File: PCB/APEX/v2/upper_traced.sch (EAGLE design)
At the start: 9 parts

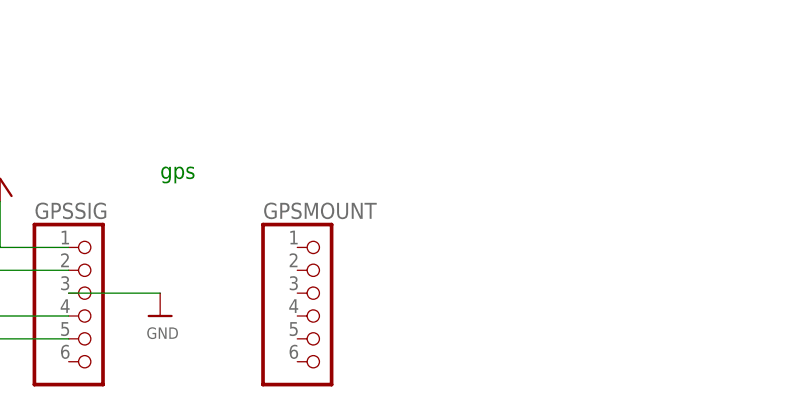
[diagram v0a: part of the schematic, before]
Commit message: realign sim
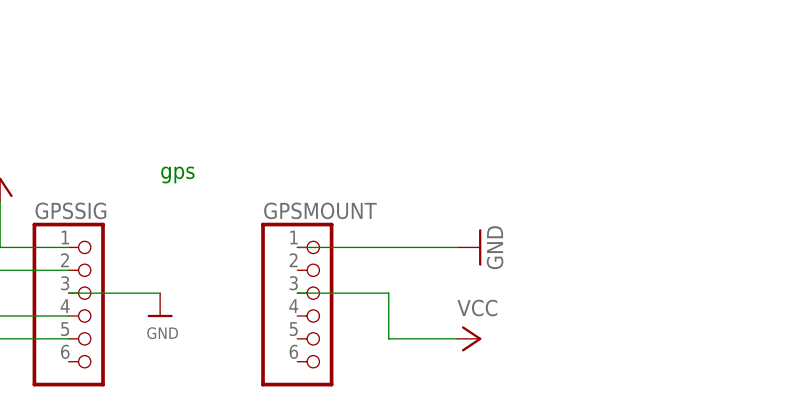
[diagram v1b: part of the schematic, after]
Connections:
- net GND: now also GPSMOUNT.1
- net VCC: now also GPSMOUNT.3
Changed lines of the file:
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@@
 <part name="GND" library="wirepad" library_urn="urn:adsk.eagle:library:412" deviceset="3,17/1,1" device="" package3d_urn="urn:adsk.eagle:package:30832/1"/>
 <part name="VCC" library="wirepad" library_urn="urn:adsk.eagle:library:412" deviceset="3,17/1,1" device="" package3d_urn="urn:adsk.eagle:package:30832/1"/>
+<part name="GND2" library="supply1" library_urn="urn:adsk.eagle:library:371" deviceset="GND" device=""/>
+<part name="P+5" library="supply1" library_urn="urn:adsk.eagle:library:371" deviceset="VCC" device=""/>
 </parts>
 <sheets>
@@
 <attribute name="VALUE" x="39.497" y="1.778" size="1.778" layer="96"/>
 </instance>
+<instance part="GND2" gate="1" x="142.24" y="-7.62" smashed="yes" rot="R90">
+<attribute name="VALUE" x="144.78" y="-10.16" size="1.778" layer="96" rot="R90"/>
+</instance>
+<instance part="P+5" gate="VCC" x="142.24" y="-17.78" smashed="yes" rot="R270">
+<attribute name="VALUE" x="139.7" y="-15.24" size="1.778" layer="96"/>
+</instance>
 </instances>
 <busses>
@@
 <wire x1="43.18" y1="10.16" x2="48.26" y2="10.16" width="0.1524" layer="91"/>
 </segment>
+<segment>
+<pinref part="GND2" gate="1" pin="GND"/>
+<pinref part="GPSMOUNT" gate="A" pin="1"/>
+<wire x1="139.7" y1="-7.62" x2="121.92" y2="-7.62" width="0.1524" layer="91"/>
+</segment>
 </net>
 <net name="VCC" class="2">
@@
 <wire x1="43.18" y1="5.08" x2="48.26" y2="5.08" width="0.1524" layer="91"/>
 </segment>
+<segment>
+<pinref part="P+5" gate="VCC" pin="VCC"/>
+<wire x1="139.7" y1="-17.78" x2="132.08" y2="-17.78" width="0.1524" layer="91"/>
+<wire x1="132.08" y1="-17.78" x2="132.08" y2="-12.7" width="0.1524" layer="91"/>
+<pinref part="GPSMOUNT" gate="A" pin="3"/>
+<wire x1="132.08" y1="-12.7" x2="121.92" y2="-12.7" width="0.1524" layer="91"/>
+</segment>
 </net>
